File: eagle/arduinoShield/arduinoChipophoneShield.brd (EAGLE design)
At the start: 101.6 x 53.3 mm, 29 parts

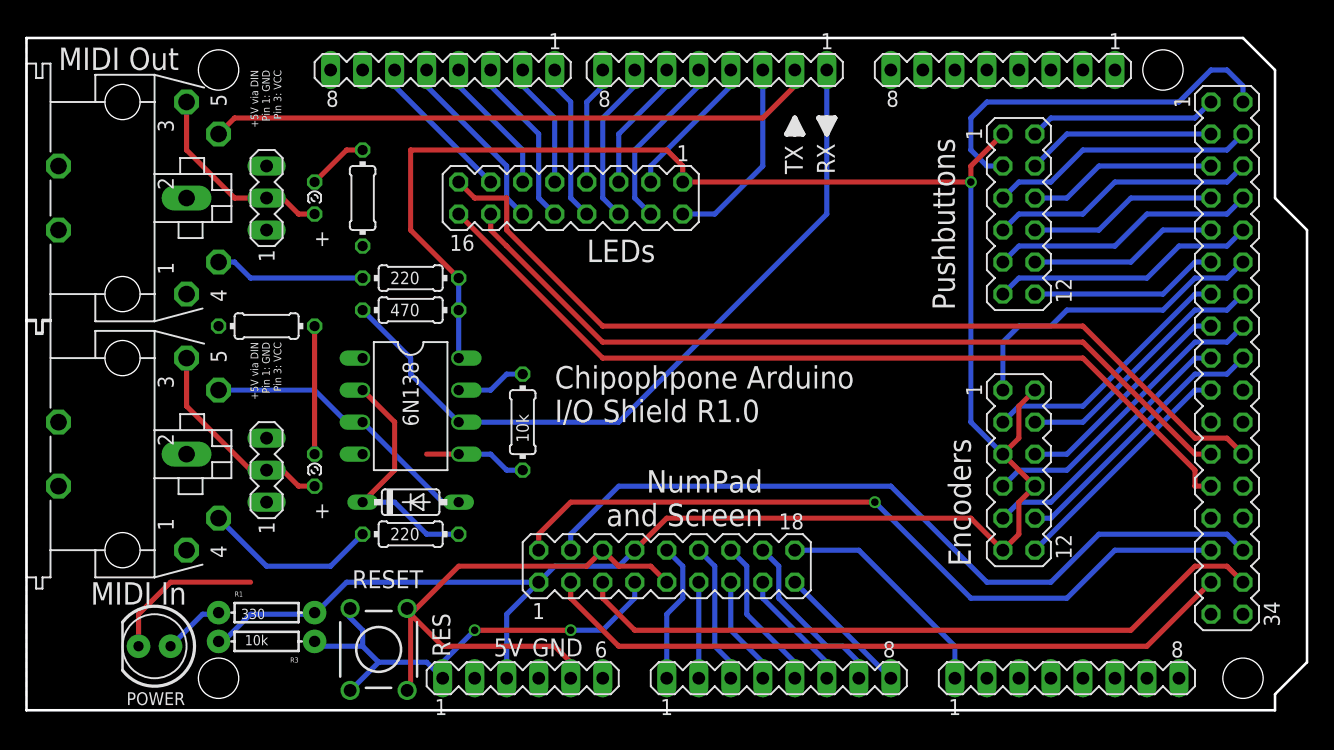
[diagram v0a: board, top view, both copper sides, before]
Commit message: Ripped up unnecessary traces due to ground/power planes. Also switched encoder common to ground to use internal pullup resistors
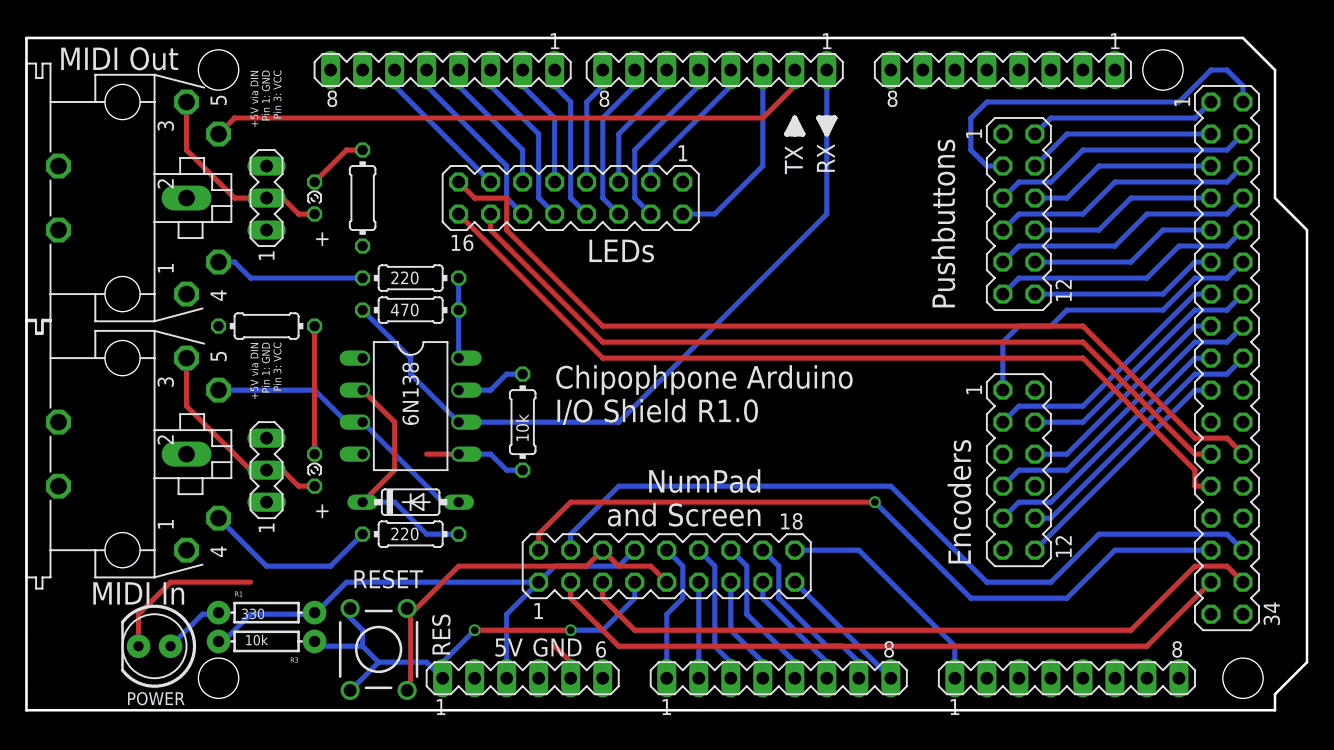
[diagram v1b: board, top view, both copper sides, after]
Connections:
- net 5V: no longer ENCODERS.11, ENCODERS.2, ENCODERS.5, ENCODERS.8
- net GND: now also ENCODERS.11, ENCODERS.2, ENCODERS.5, ENCODERS.8
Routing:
- net 5V: track 183.9 -> 51.2 mm, vias 1 -> 0
- net GND: track 64.7 -> 52.3 mm
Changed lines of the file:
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@@
 <contactref element="R3" pad="P$2"/>
 <contactref element="R1" pad="P$2"/>
-<contactref element="ENCODERS" pad="2"/>
-<contactref element="ENCODERS" pad="5"/>
-<contactref element="ENCODERS" pad="8"/>
-<contactref element="ENCODERS" pad="11"/>
 <contactref element="PUSHBUTTONS" pad="1"/>
 <contactref element="LED" pad="1"/>
 <contactref element="SCREEN_NUMPAD" pad="1"/>
 <contactref element="SCREEN_NUMPAD" pad="8"/>
-<wire x1="80.01" y1="25.4" x2="78.74" y2="24.13" width="0.4064" layer="1"/>
-<wire x1="78.74" y1="24.13" x2="78.74" y2="21.59" width="0.4064" layer="1"/>
-<wire x1="78.74" y1="21.59" x2="77.47" y2="20.32" width="0.4064" layer="1"/>
-<wire x1="77.47" y1="20.32" x2="80.01" y2="17.78" width="0.4064" layer="1"/>
-<wire x1="80.01" y1="17.78" x2="78.74" y2="16.51" width="0.4064" layer="1"/>
-<wire x1="78.74" y1="16.51" x2="78.74" y2="13.97" width="0.4064" layer="1"/>
-<wire x1="78.74" y1="13.97" x2="77.47" y2="12.7" width="0.4064" layer="1"/>
-<wire x1="74.93" y1="41.91" x2="74.93" y2="43.18" width="0.4064" layer="1"/>
-<wire x1="74.93" y1="43.18" x2="77.47" y2="45.72" width="0.4064" layer="1"/>
-<wire x1="52.07" y1="41.91" x2="74.93" y2="41.91" width="0.4064" layer="1"/>
-<wire x1="48.26" y1="12.7" x2="50.8" y2="15.24" width="0.4064" layer="1"/>
 <wire x1="40.64" y1="10.16" x2="38.1" y2="7.62" width="0.4064" layer="16"/>
-<wire x1="50.8" y1="15.24" x2="74.93" y2="15.24" width="0.4064" layer="1"/>
-<wire x1="74.93" y1="15.24" x2="77.47" y2="12.7" width="0.4064" layer="1"/>
 <wire x1="48.26" y1="12.7" x2="46.99" y2="11.43" width="0.4064" layer="16"/>
 <wire x1="46.99" y1="11.43" x2="41.91" y2="11.43" width="0.4064" layer="16"/>
 <wire x1="41.91" y1="11.43" x2="40.64" y2="10.16" width="0.4064" layer="16"/>
-<via x="74.93" y="41.91" extent="1-16" drill="0.6" shape="square"/>
-<wire x1="74.93" y1="41.91" x2="74.93" y2="22.86" width="0.4064" layer="16"/>
-<wire x1="74.93" y1="22.86" x2="77.47" y2="20.32" width="0.4064" layer="16"/>
 <wire x1="40.64" y1="10.16" x2="25.4" y2="10.16" width="0.4064" layer="16"/>
 <wire x1="25.4" y1="10.16" x2="22.86" y2="7.62" width="0.4064" layer="16"/>
@@
 <wire x1="34.29" y1="27.94" x2="34.29" y2="31.75" width="0.4064" layer="16"/>
 <wire x1="34.29" y1="31.75" x2="34.29" y2="34.29" width="0.4064" layer="16"/>
-<wire x1="34.29" y1="34.29" x2="30.48" y2="38.1" width="0.4064" layer="1"/>
-<wire x1="30.48" y1="38.1" x2="30.48" y2="44.45" width="0.4064" layer="1"/>
-<wire x1="30.48" y1="44.45" x2="50.8" y2="44.45" width="0.4064" layer="1"/>
-<wire x1="50.8" y1="44.45" x2="52.07" y2="43.18" width="0.4064" layer="1"/>
-<wire x1="52.07" y1="43.18" x2="52.07" y2="41.91" width="0.4064" layer="1"/>
 <contactref element="SV4" pad="1"/>
 <contactref element="SV3" pad="1"/>
@@
 <contactref element="SCREEN_NUMPAD" pad="9"/>
 <wire x1="43.18" y1="3.81" x2="41.91" y2="5.08" width="0.4064" layer="1"/>
-<wire x1="41.91" y1="5.08" x2="33.02" y2="5.08" width="0.4064" layer="1"/>
-<wire x1="33.02" y1="5.08" x2="30.48" y2="7.62" width="0.4064" layer="1"/>
 <wire x1="30.48" y1="7.62" x2="30.48" y2="1.27" width="0.4064" layer="1"/>
 <wire x1="45.72" y1="12.7" x2="44.45" y2="11.43" width="0.4064" layer="1"/>
@@
 <vertex x="96.52" y="53.34"/>
 </polygon>
+<contactref element="ENCODERS" pad="2"/>
+<contactref element="ENCODERS" pad="8"/>
+<contactref element="ENCODERS" pad="5"/>
+<contactref element="ENCODERS" pad="11"/>
 </signal>
 <signal name="A0">

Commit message: R 1.1, with Encoder common to ground, and moved switches and LEDs for easier attachment
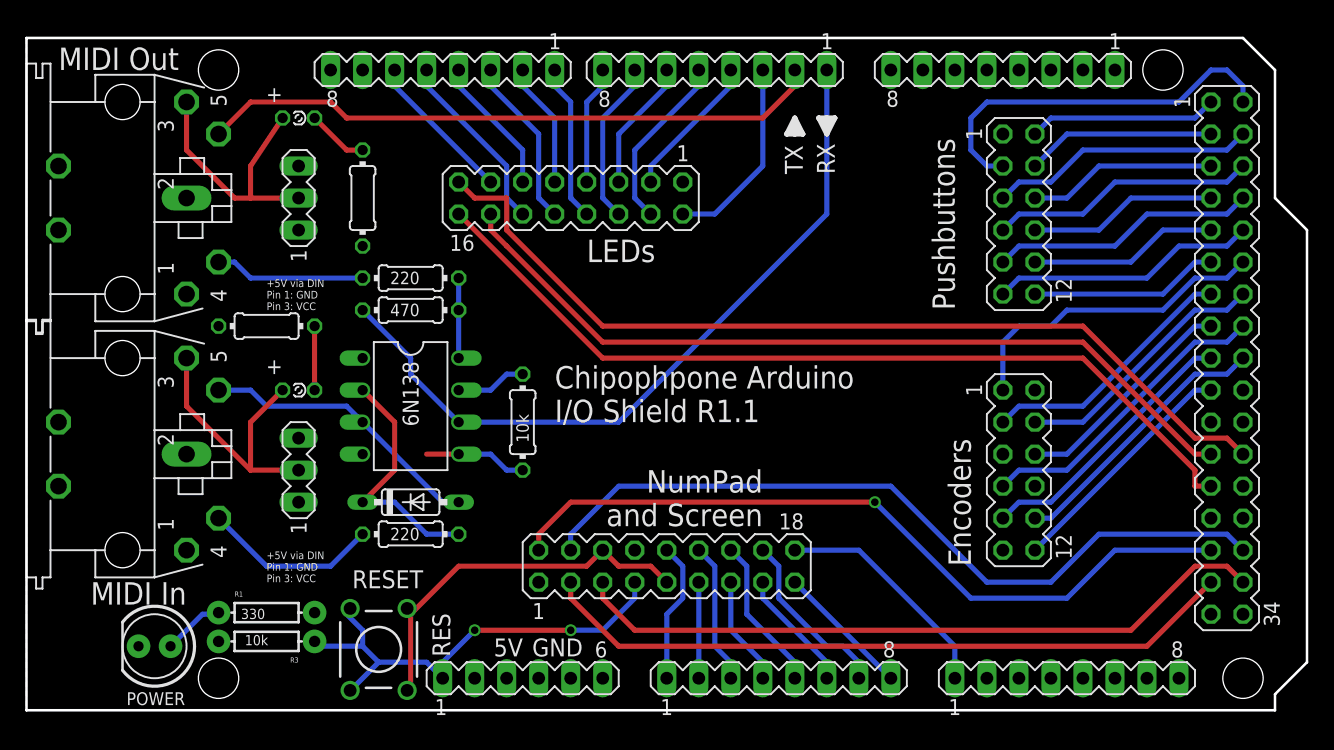
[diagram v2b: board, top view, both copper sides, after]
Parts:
- moved LED2 6.48 mm to (21.6, 47.0), turned to 0 degrees
- moved LED3 6.48 mm to (21.6, 25.4), turned to 0 degrees
- moved SV3 2.54 mm to (21.6, 40.6)
- moved SV4 2.54 mm to (21.6, 19.1)
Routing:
- net 5V: track 51.2 -> 6.35 mm
- net GND: track 52.3 -> 38.0 mm
- net N$1: track 16.6 -> 23.5 mm
- net N$2: track 16.1 -> 22.7 mm
- net N$13: track 10.2 -> 5.08 mm
- net N$7: track 22.7 -> 24.0 mm
- net TX1: track 48.6 -> 49.6 mm
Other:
- board text added: "Chipophpone Arduino I/O Shield R1.1"
- board text removed: "Chipophpone Arduino I/O Shield R1.0"

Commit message: Updated so switches can also use internal pullup resistors
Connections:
- net 5V: no longer PUSHBUTTONS.1
- net GND: now also PUSHBUTTONS.1
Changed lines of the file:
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@@
 <contactref element="R3" pad="P$2"/>
 <contactref element="R1" pad="P$2"/>
-<contactref element="PUSHBUTTONS" pad="1"/>
 <contactref element="LED" pad="1"/>
 <contactref element="SCREEN_NUMPAD" pad="1"/>
@@
 <contactref element="ENCODERS" pad="5"/>
 <contactref element="ENCODERS" pad="11"/>
+<contactref element="PUSHBUTTONS" pad="1"/>
 </signal>
 <signal name="A0">
